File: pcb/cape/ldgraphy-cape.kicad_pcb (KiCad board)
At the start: 2 copper layers, 19 parts, among them P1 12V, P2 Laser, P4 Stepper, P5 CONN_01X05, P8 BB_P8, P9 BB_P9, Q1 BC237, Q2 BD135, Q3 MTM232270, U1 POLOLUSTEPPER

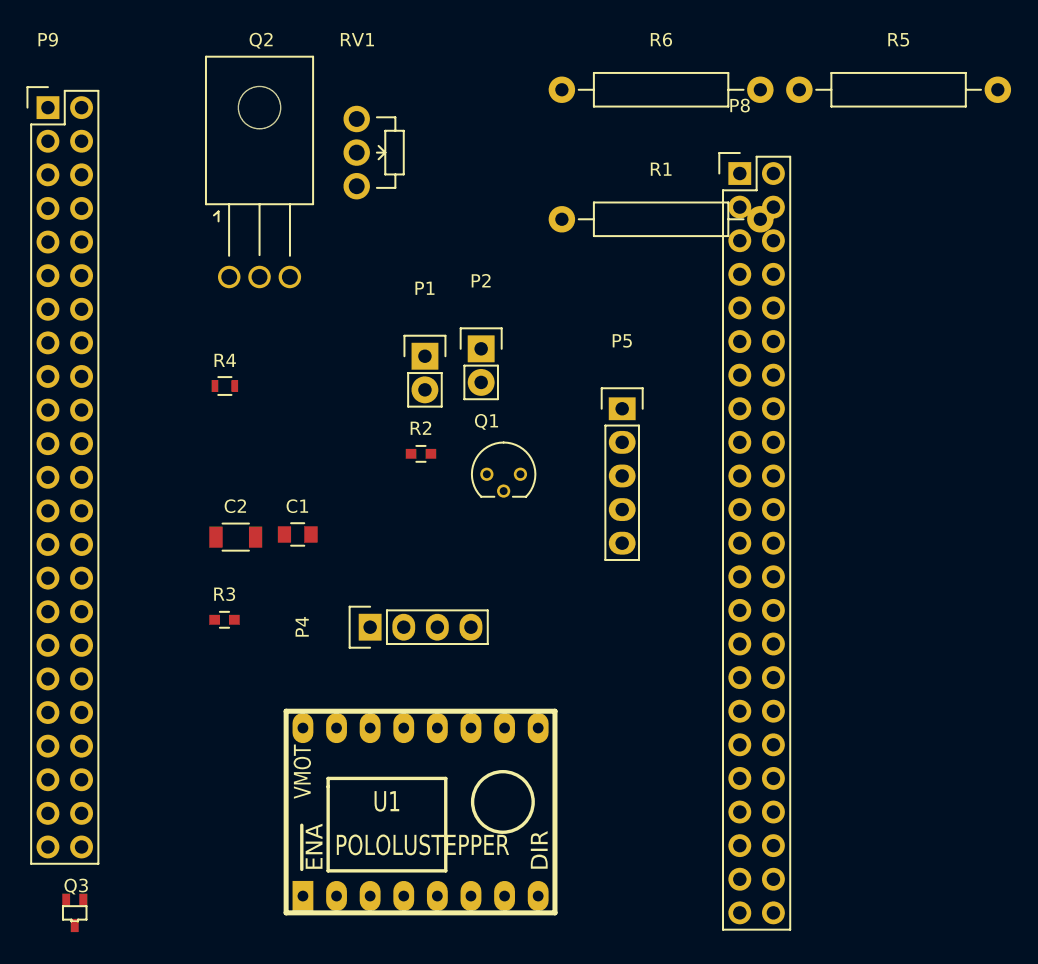
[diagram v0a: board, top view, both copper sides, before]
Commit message: o Update cape: include hsync circuit o Laser driver: new board that uses the new OpAmp circuit   (not tested yet)
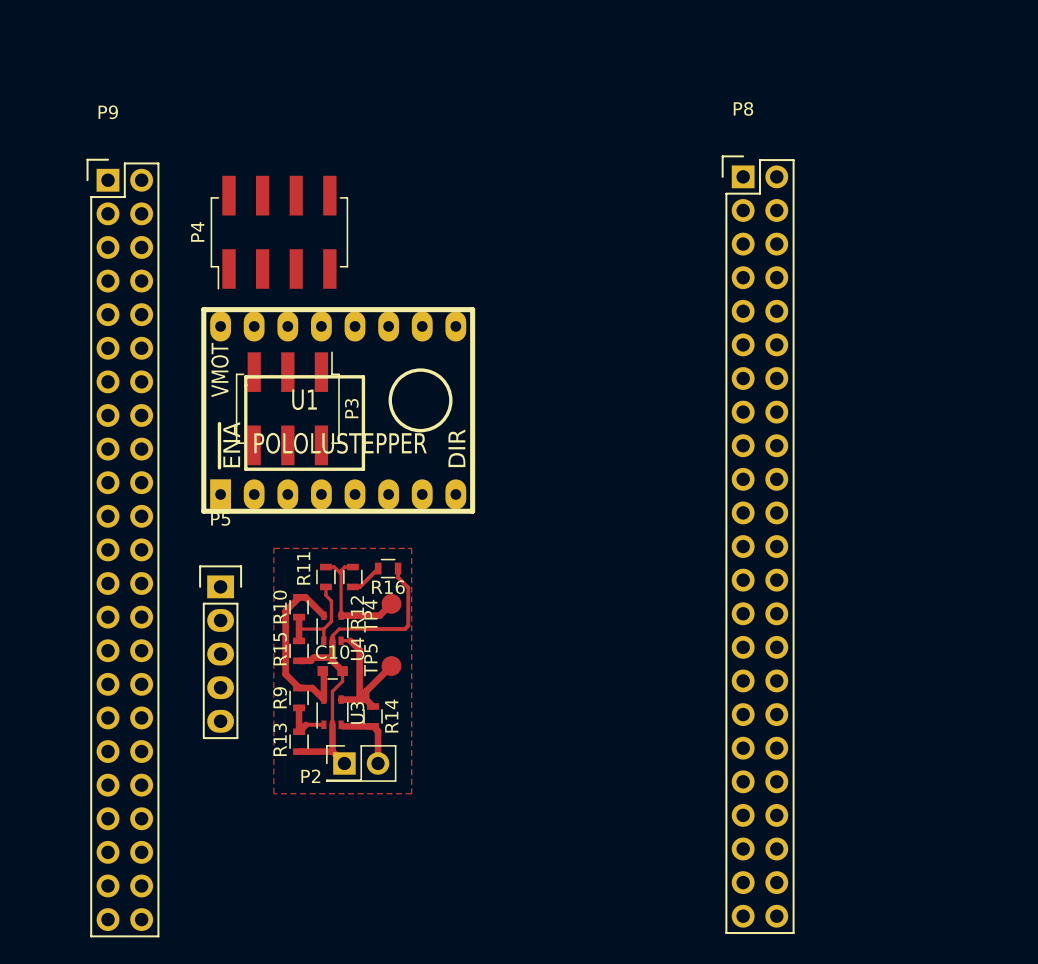
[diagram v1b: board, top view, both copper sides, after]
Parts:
- removed C1: 100n, Capacitors_SMD:C_0805
- removed C2: 10u, Capacitors_SMD:C_1206
- removed P1: 12V, Pin_Headers:Pin_Header_Straight_1x02
- removed Q1: BC237, TO_SOT_Packages_THT:TO-92_Molded_Narrow_Reverse
- removed Q2: BD135, TO_SOT_Packages_THT:SOT126_SOT32_Housing_Horizontal
- removed Q3: MTM232270, TO_SOT_Packages_SMD:SOT-323
- removed R1: R, Resistors_ThroughHole:Resistor_Horizontal_RM15mm
- removed R2, R3: R, Capacitors_SMD:C_0603
- removed R4: 100, Resistors_SMD:R_0603
- removed R5: 4R7, Resistors_ThroughHole:Resistor_Horizontal_RM15mm
- removed R6: 470, Resistors_ThroughHole:Resistor_Horizontal_RM15mm
- removed RV1: POT, Potentiometers:Potentiometer_WirePads_Small
- added C10: C, Capacitors_SMD:C_0603, F.Cu at (91.1, 82.1)
- added P3: Jumper, Pin_Headers:Pin_Header_Straight_2x03_Pitch2.54mm_SMD, F.Cu at (87.8, 62.2)
- added R10: R, Resistors_SMD:R_0603, F.Cu at (88.6, 77.2)
- added R11: R, Resistors_SMD:R_0603, F.Cu at (90.6, 74.9)
- added R12: 1k, Resistors_SMD:R_0603, F.Cu at (92.7, 74.9)
- added R13: R, Resistors_SMD:R_0603, F.Cu at (88.6, 87.4)
- added R14: R, Resistors_SMD:R_0603, F.Cu at (94.2, 85.5)
- added R15: R, Resistors_SMD:R_0603, F.Cu at (88.6, 80.5)
- added R16: 2k2, Resistors_SMD:R_0603, F.Cu at (95.3, 74.3)
- added R9: R, Resistors_SMD:R_0603, F.Cu at (88.6, 84.1)
- added TP4: HSync, Measurement_Points:Measurement_Point_Round-SMD-Pad_Small, F.Cu at (95.6, 77.0)
- added TP5: VPhoto, Measurement_Points:Measurement_Point_Round-SMD-Pad_Small, F.Cu at (95.6, 81.7)
- added U3: MIC920, TO_SOT_Packages_SMD:SOT-353_SC-70-5, F.Cu at (91.1, 85.2)
- added U4: MIC920, TO_SOT_Packages_SMD:SOT-353_SC-70-5, F.Cu at (91.1, 78.8)
- P2: value Laser -> PhDiode; footprint Pin_Headers:Pin_Header_Straight_1x02 -> Pin_Headers:Pin_Header_Straight_2x01_Pitch2.54mm
- P4: value Stepper -> CONN_02X04; footprint Pin_Headers:Pin_Header_Straight_1x04 -> Pin_Headers:Pin_Header_Straight_2x04_Pitch2.54mm_SMD
- moved P5 33.2 mm to (82.7, 75.7)
- moved P2 33.0 mm to (92.0, 89.0)
- moved U1 31.0 mm to (91.6, 64.9)
- moved P4 30.6 mm to (87.1, 48.9)
- moved P9 7.12 mm to (74.2, 45.0)
- moved P8 0.36 mm to (122.2, 44.7)
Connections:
- P2 pad 1: Net-(P2-Pad1) -> GND
- P4 pad 1: Net-(P4-Pad1) -> (no net)
- P4 pad 2: Net-(P4-Pad2) -> (no net)
- P4 pad 3: Net-(P4-Pad3) -> GND
- P4 pad 4: Net-(P4-Pad4) -> GND
- P5 pad 2: Net-(P5-Pad2) -> (no net)
- P5 pad 3: GND -> ~MOTORS_EN
- P8 pad 1: Net-(P8-Pad1) -> (no net)
- P8 pad 10: Net-(P8-Pad10) -> (no net)
- P8 pad 11: Net-(P8-Pad11) -> (no net)
- P8 pad 12: Net-(P8-Pad12) -> (no net)
- P8 pad 13: Net-(P8-Pad13) -> (no net)
- P8 pad 14: Net-(P8-Pad14) -> (no net)
- P8 pad 15: Net-(P8-Pad15) -> (no net)
- P8 pad 16: Net-(P8-Pad16) -> (no net)
- P8 pad 17: Net-(P8-Pad17) -> (no net)
- P8 pad 18: Net-(P8-Pad18) -> (no net)
- P8 pad 19: Net-(P8-Pad19) -> (no net)
- P8 pad 2: Net-(P8-Pad2) -> (no net)
- P8 pad 20: Net-(P8-Pad20) -> (no net)
- P8 pad 21: Net-(P8-Pad21) -> (no net)
- P8 pad 22: Net-(P8-Pad22) -> (no net)
- P8 pad 23: Net-(P8-Pad23) -> (no net)
- P8 pad 24: Net-(P8-Pad24) -> (no net)
- P8 pad 25: Net-(P8-Pad25) -> (no net)
- P8 pad 26: Net-(P8-Pad26) -> (no net)
- P8 pad 27: Net-(P8-Pad27) -> (no net)
- P8 pad 28: Net-(P8-Pad28) -> (no net)
- P8 pad 29: Net-(P8-Pad29) -> (no net)
- P8 pad 3: Net-(P8-Pad3) -> (no net)
- P8 pad 30: Net-(P8-Pad30) -> (no net)
- P8 pad 31: Net-(P8-Pad31) -> (no net)
- P8 pad 32: Net-(P8-Pad32) -> (no net)
- P8 pad 33: Net-(P8-Pad33) -> (no net)
- P8 pad 34: Net-(P8-Pad34) -> (no net)
- P8 pad 35: Net-(P8-Pad35) -> (no net)
- P8 pad 36: Net-(P8-Pad36) -> (no net)
- P8 pad 37: Net-(P8-Pad37) -> (no net)
- P8 pad 38: Net-(P8-Pad38) -> (no net)
- P8 pad 39: Net-(P8-Pad39) -> (no net)
- P8 pad 4: Net-(P8-Pad4) -> (no net)
- P8 pad 40: Net-(P8-Pad40) -> (no net)
- P8 pad 41: Net-(P8-Pad41) -> (no net)
- P8 pad 42: Net-(P8-Pad42) -> (no net)
- P8 pad 43: Net-(P8-Pad43) -> (no net)
- P8 pad 44: Net-(P8-Pad44) -> (no net)
- P8 pad 45: Net-(P8-Pad45) -> (no net)
- P8 pad 46: Net-(P8-Pad46) -> (no net)
- P8 pad 5: Net-(P8-Pad5) -> (no net)
- P8 pad 6: Net-(P8-Pad6) -> (no net)
- P8 pad 7: Net-(P8-Pad7) -> (no net)
- P8 pad 8: Net-(P8-Pad8) -> (no net)
- P8 pad 9: Net-(P8-Pad9) -> (no net)
- P9 pad 10: Net-(P9-Pad10) -> (no net)
- P9 pad 11: Net-(P9-Pad11) -> (no net)
- P9 pad 12: Net-(P9-Pad12) -> (no net)
- P9 pad 13: SLED_STEP -> ~MOTORS_EN
- P9 pad 14: ~SLED_EN -> SLED_STEP
- P9 pad 16: Net-(P9-Pad16) -> (no net)
- P9 pad 17: LASER_DATA -> (no net)
- P9 pad 19: Net-(P9-Pad19) -> (no net)
- P9 pad 20: Net-(P9-Pad20) -> (no net)
- P9 pad 21: Net-(P9-Pad21) -> (no net)
- P9 pad 22: Net-(P9-Pad22) -> (no net)
- P9 pad 23: Net-(P9-Pad23) -> (no net)
- P9 pad 24: Net-(P9-Pad24) -> (no net)
- P9 pad 25: Net-(P9-Pad25) -> (no net)
- P9 pad 26: Net-(P9-Pad26) -> (no net)
- P9 pad 27: Net-(P9-Pad27) -> (no net)
- P9 pad 28: Net-(P9-Pad28) -> (no net)
- P9 pad 29: Net-(P9-Pad29) -> (no net)
- P9 pad 30: Net-(P9-Pad30) -> (no net)
- P9 pad 31: Net-(P9-Pad31) -> (no net)
- P9 pad 32: Net-(P9-Pad32) -> (no net)
- P9 pad 33: Net-(P9-Pad33) -> (no net)
- P9 pad 34: Net-(P9-Pad34) -> (no net)
- P9 pad 35: Net-(P9-Pad35) -> (no net)
- P9 pad 36: Net-(P9-Pad36) -> (no net)
- P9 pad 37: Net-(P9-Pad37) -> (no net)
- P9 pad 38: Net-(P9-Pad38) -> (no net)
- P9 pad 39: Net-(P9-Pad39) -> (no net)
- P9 pad 40: Net-(P9-Pad40) -> (no net)
- P9 pad 41: Net-(P9-Pad41) -> (no net)
- P9 pad 42: Net-(P9-Pad42) -> (no net)
- P9 pad 43: Net-(P9-Pad43) -> (no net)
- P9 pad 44: Net-(P9-Pad44) -> (no net)
- P9 pad 45: Net-(P9-Pad45) -> (no net)
- P9 pad 46: Net-(P9-Pad46) -> (no net)
- P9 pad 5: Net-(P9-Pad5) -> (no net)
- P9 pad 6: Net-(P9-Pad6) -> (no net)
- P9 pad 7: Net-(P9-Pad7) -> +5V
- P9 pad 8: Net-(P9-Pad8) -> +5V
- P9 pad 9: Net-(P9-Pad9) -> (no net)
- U1 pad 1: ~SLED_EN -> ~MOTORS_EN
- U1 pad 11: Net-(P4-Pad4) -> Net-(P4-Pad6)
- U1 pad 12: Net-(P4-Pad3) -> Net-(P4-Pad8)
- U1 pad 13: Net-(P4-Pad2) -> Net-(P4-Pad7)
- U1 pad 14: Net-(P4-Pad1) -> Net-(P4-Pad5)
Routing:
- net GND: track 0.00 -> 26.5 mm
- net +5V: track 0.00 -> 14.6 mm
- net /VPhoto: track 0.00 -> 11.4 mm
- net /HSyncTrig: track 0.00 -> 9.94 mm
- net Net-(R10-Pad2): track 0.00 -> 8.16 mm
- net Net-(P2-Pad2): track 0.00 -> 5.26 mm
- net Net-(R13-Pad1): track 0.00 -> 3.89 mm
- net Net-(R12-Pad1): track 0.00 -> 2.49 mm
- added copper zone on F.Cu, net GND
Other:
- net class Default: clearance 0.2 -> 0.19; via_dia 0.8 -> 2; via_drill 0.4 -> 0.8
- net class Power added: clearance 0.5, trace_width 0.5, via_dia 2, via_drill 0.8
- rule trace_clearance: 0.2 -> 0.19

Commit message: o Sketch out cape. NB: different GPIO assignment than   current software expects.
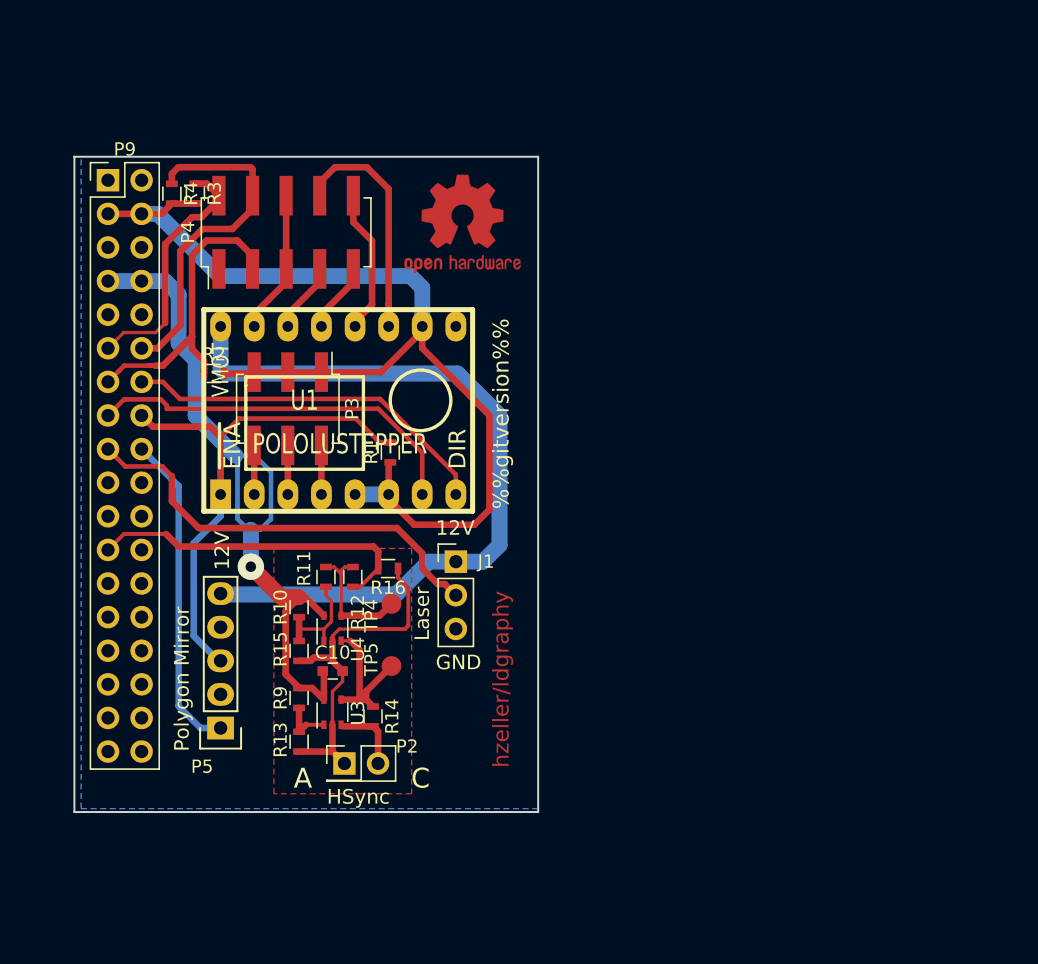
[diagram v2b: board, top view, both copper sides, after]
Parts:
- removed P8: BB_P8, Pin_Headers:Pin_Header_Straight_2x23
- added J1: CONN_01X03, Pin_Headers:Pin_Header_Straight_1x03_Pitch2.54mm, F.Cu at (100.5, 73.8)
- added R1: 4k7, Resistors_SMD:R_0603, F.Cu at (95.5, 65.5)
- added R2: 1k, Resistors_SMD:R_0603, F.Cu at (82.2, 59.6)
- added R3: 1k, Resistors_SMD:R_0603, F.Cu at (80.8, 46.0)
- added R4: 1k, Resistors_SMD:R_0603, F.Cu at (79.0, 46.0)
- added REF***: OSHW-Logo2_9.8x8mm_Copper, Symbols:OSHW-Logo2_9.8x8mm_Copper, F.Cu at (101.0, 48.3)
- P4: value CONN_02X04 -> BaseConn; footprint Pin_Headers:Pin_Header_Straight_2x04_Pitch2.54mm_SMD -> Pin_Headers:Pin_Header_Straight_2x05_Pitch2.54mm_SMD
- P9: footprint Pin_Headers:Pin_Header_Straight_2x23 -> Pin_Headers:Pin_Header_Straight_2x18_Pitch2.54mm
- moved P5 10.7 mm to (82.7, 86.4), turned to 180 degrees
- moved P4 0.51 mm to (87.6, 48.9)
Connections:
- P4 pad 2: (no net) -> ~UI-Button
- P4 pad 3: GND -> ~StopFront
- P4 pad 4: GND -> ~StopBack
- P4 pad 5: Net-(P4-Pad5) -> GND
- P4 pad 6: Net-(P4-Pad6) -> GND
- P9 pad 11: (no net) -> ~UI-Button
- P9 pad 12: (no net) -> ~StopBack
- P9 pad 13: ~MOTORS_EN -> ~StopFront
- P9 pad 14: SLED_STEP -> SLED_DIR
- P9 pad 15: SLED_DIR -> SLED_STEP
- P9 pad 16: (no net) -> ~MOTORS_EN
- P9 pad 17: (no net) -> LASER_DATA
- P9 pad 23: (no net) -> Hsync
- R12 pad 1: Net-(R12-Pad1) -> Hsync
- R16 pad 2: Net-(R12-Pad1) -> Hsync
- U1 pad 11: Net-(P4-Pad6) -> Net-(P4-Pad8)
- U1 pad 12: Net-(P4-Pad8) -> Net-(P4-Pad10)
- U1 pad 13: Net-(P4-Pad7) -> Net-(P4-Pad9)
- U1 pad 14: Net-(P4-Pad5) -> Net-(P4-Pad7)
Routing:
- net 3.3V: track 0.00 -> 80.8 mm
- net +12V: track 0.00 -> 58.3 mm
- net +5V: track 14.6 -> 57.2 mm, vias 0 -> 1
- net ~MOTORS_EN: track 0.00 -> 40.0 mm
- net LASER_DATA: track 0.00 -> 32.7 mm
- net SLED_STEP: track 0.00 -> 29.2 mm
- net SLED_DIR: track 0.00 -> 28.1 mm
- net ~StopBack: track 0.00 -> 27.2 mm
- net Hsync: track 0.00 -> 25.3 mm
- net MIRROR_CLK: track 0.00 -> 24.6 mm
- net ~StopFront: track 0.00 -> 24.6 mm
- net ~UI-Button: track 0.00 -> 20.3 mm
- net Net-(P4-Pad8): track 0.00 -> 17.8 mm
- net Net-(P4-Pad10): track 0.00 -> 11.0 mm
- net GND: track 26.5 -> 37.4 mm
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- added copper zone on B.Cu, net GND
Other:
- board outline added: 35.1 x 49.5 mm
- net class Default: trace_width 0.25 -> 0.3
- board text added: "%%gitversion%%"
- board text added: "12V"
- board text added: "A"
- board text added: "C"
- board text added: "GND"
- board text added: "HSync"
- board text added: "Laser"
- board text added: "Polygon Mirror"
- board text added: "hzeller/ldgraphy"

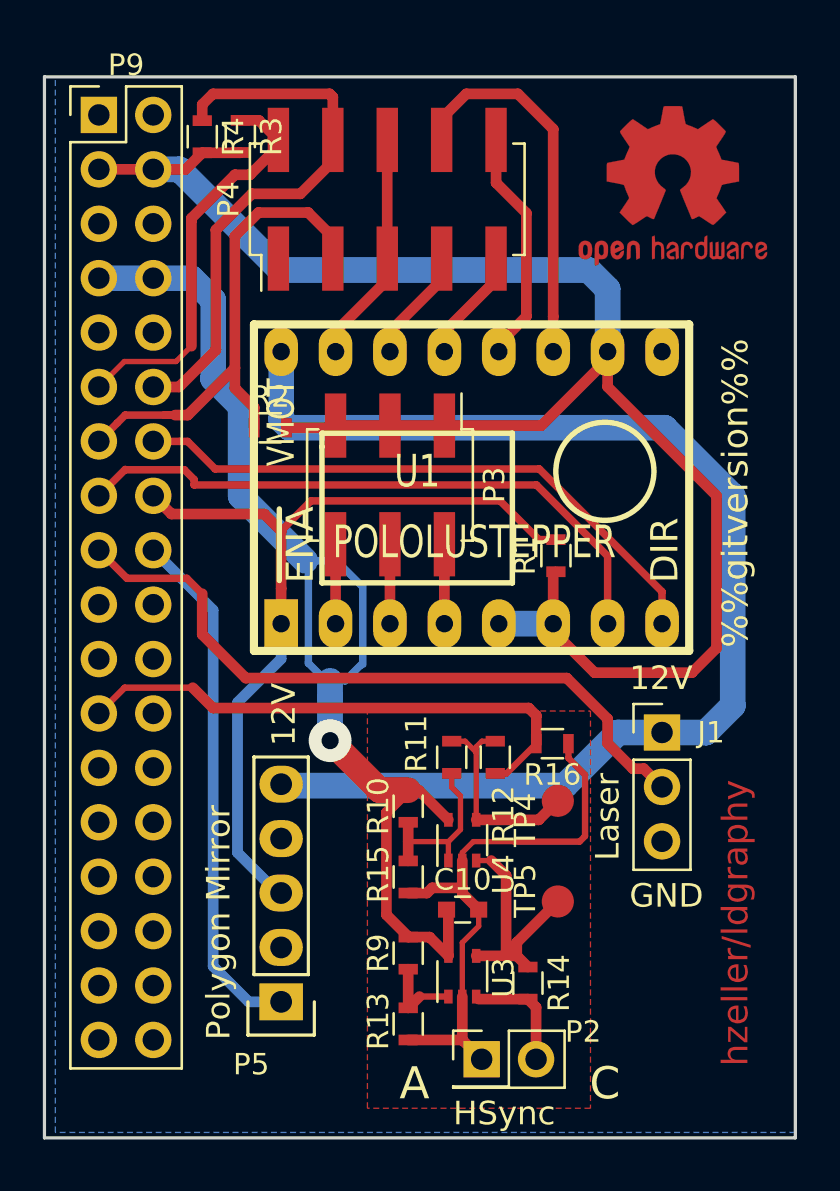
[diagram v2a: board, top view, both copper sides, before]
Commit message: o Add DC/DC converter to cape.
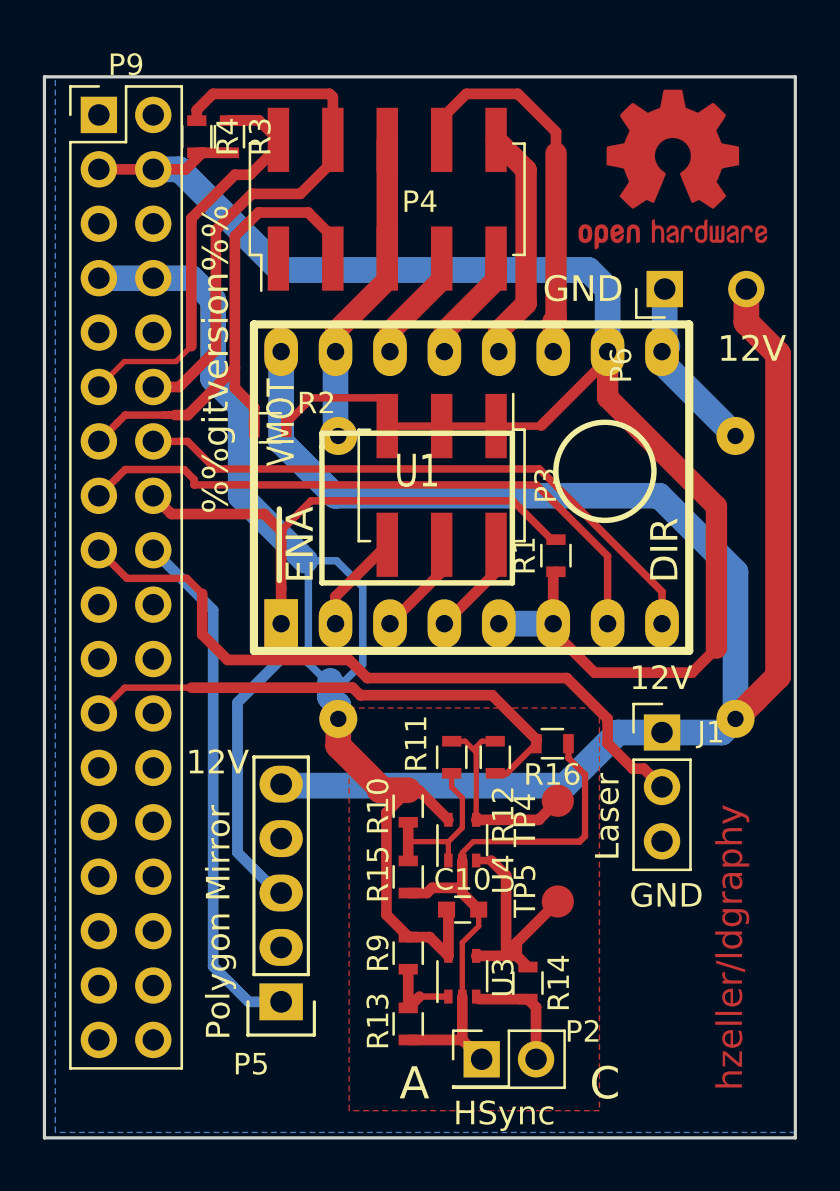
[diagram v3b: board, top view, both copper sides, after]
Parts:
- added P6: 12V-in, Pin_Headers:Pin_Header_Straight_1x02_Pitch2.54mm, F.Cu at (100.6, 53.1)
- added U2: DCDC1584, ldgraphy:dcdc-mp1584, B.Cu at (94.6, 66.5)
- moved P3 2.41 mm to (90.2, 62.3)
- moved REF*** 0.76 mm to (101.0, 47.5)
- moved R3 0.51 mm to (80.3, 46.0)
- moved R4 0.25 mm to (78.7, 46.0)
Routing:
- net +12V: track 58.3 -> 78.8 mm
- net GND: track 37.4 -> 50.1 mm
- net 3.3V: track 80.8 -> 82.5 mm
- net (no net): track 1.00 -> 0.00 mm
- net Net-(P3-Pad6): track 3.71 -> 4.68 mm
- net Net-(P3-Pad4): track 3.71 -> 4.68 mm
- net Net-(P3-Pad2): track 3.71 -> 4.68 mm
- net ~UI-Button: track 20.3 -> 21.0 mm
- net Hsync: track 25.3 -> 24.7 mm
- net +5V: vias 1 -> 0
